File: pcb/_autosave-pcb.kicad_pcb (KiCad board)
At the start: 2 copper layers, 57 x 46 mm, 14 parts, among them J1 BMV080, J2 BATTERY_IN, J3 QWIIC, U1 ESP32-C6-WROOM-1, U2 BME680, U3 MSA311, U5 TPS63020

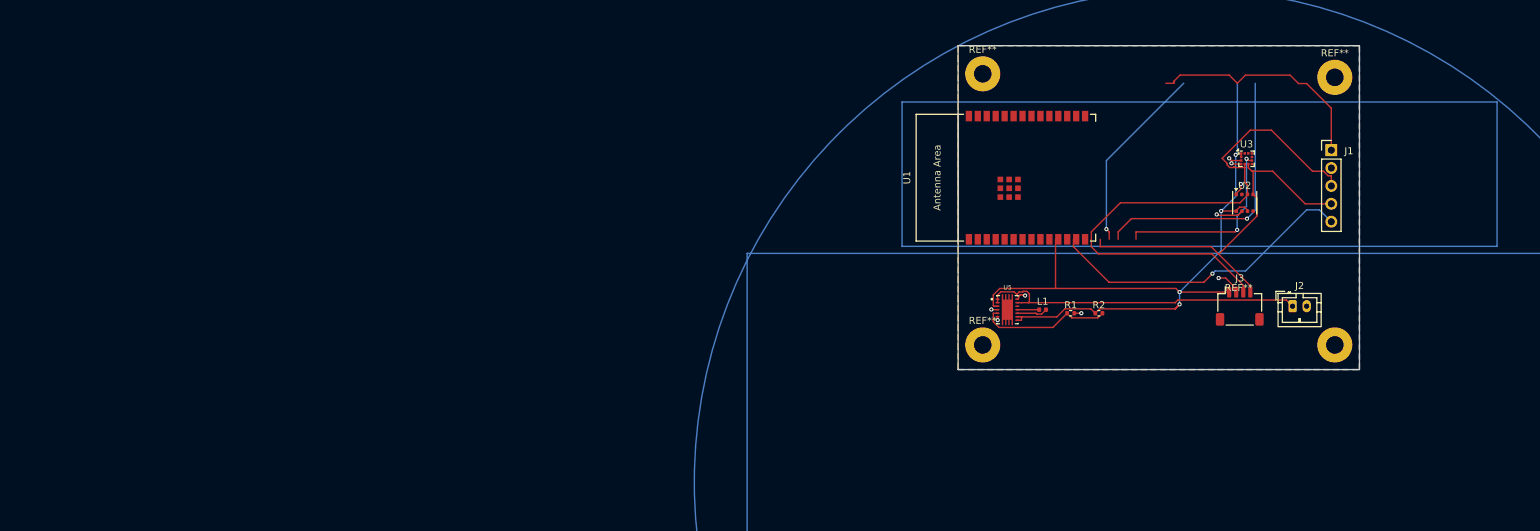
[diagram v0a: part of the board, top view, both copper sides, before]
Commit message: Add demo alert UI and skeleton map
Introduce a demo alert workflow and placeholder map state: DeviceDetailPanel now accepts isDemo, demoAlertActive and onDemoAlert and shows a dedicated "Simulate Vape Alert" / "Clear Demo Alert" action for demo devices. DeviceMap gains a forceSkeletonMap prop to force the grey/example floorplan skeleton (and hide the real SVG image) and updates the skeleton label when forced. Devices page now wires demo state into the map and detail panel and removes the previous global demo button. Also include autogenerated PCB autosave changes (footprint UUIDs/positions) and add a PCB backup zip.
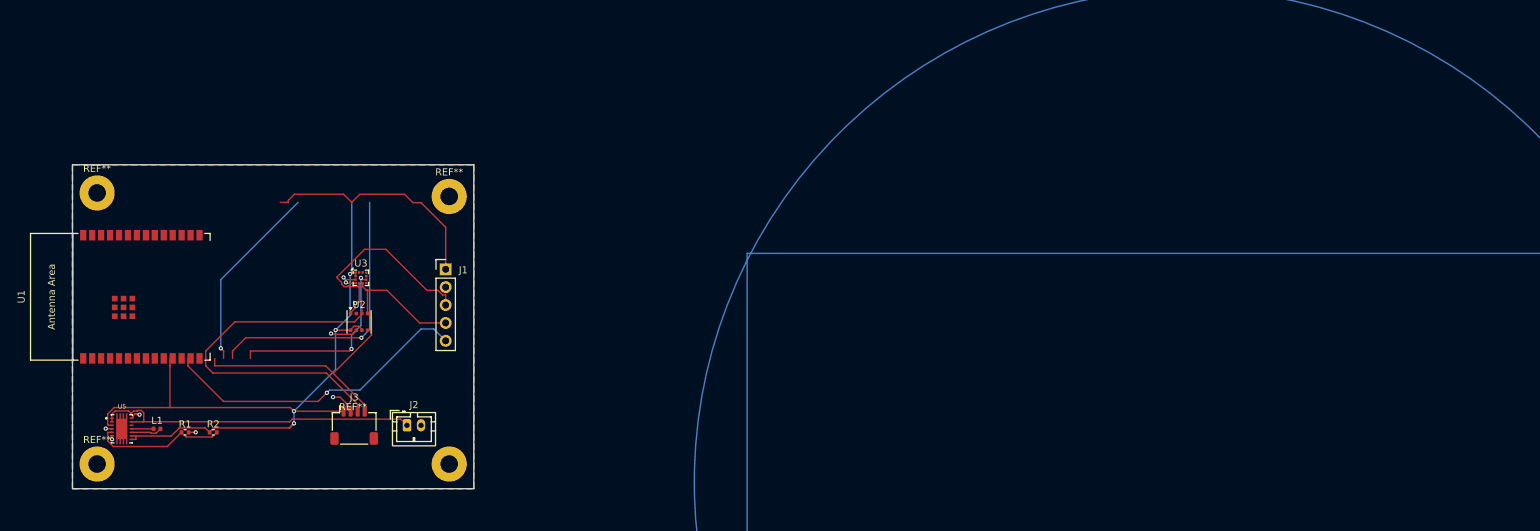
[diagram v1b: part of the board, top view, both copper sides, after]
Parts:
- moved J1 126.9 mm to (84.2, 57.8)
- moved J2 126.9 mm to (78.7, 79.9)
- moved J3 126.9 mm to (71.2, 79.9)
- moved L1 126.9 mm to (43.2, 80.4)
- moved REF** 126.9 mm to (84.7, 47.4)
- moved REF** 126.9 mm to (84.7, 85.4)
- moved REF** 126.9 mm to (34.7, 46.9)
- moved REF** 126.9 mm to (34.7, 85.4)
- moved U1 126.9 mm to (41.0, 61.7)
- moved U3 126.9 mm to (72.2, 59.0)
- moved U5 126.9 mm to (38.2, 80.4)
- moved U2 126.9 mm to (71.9, 65.2)
- moved R1 126.9 mm to (47.2, 80.9)
- moved R2 126.9 mm to (51.2, 80.9)
